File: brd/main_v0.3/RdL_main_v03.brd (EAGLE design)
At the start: 45 x 33.7 mm, 33 parts, among them U1 MPU-6000QFN-24

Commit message: Version Ready for fabrication
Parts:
- removed TEST: PRG, SparkFun-Connectors:1X01_POGOPIN_HOLE_0.58
- added J1: Test, SparkFun-Connectors:1X01
- moved COMM 25.7 mm to (23.2, 28.9)
- moved RT1 21.7 mm to (6.56, 2.50), turned to 0 degrees
- moved BSUPLY 19.6 mm to (2.48, 22.5), turned to 270 degrees
- moved RBUTTON 13.2 mm to (22.1, 19.1), turned to 90 degrees
- moved RT2 11.6 mm to (33.4, 2.28), turned to 180 degrees
- moved BUTTON 11.2 mm to (25.9, 2.50)
- moved D2 11.1 mm to (40.7, 14.2)
- moved R1T1 8.72 mm to (40.7, 8.30), turned to 270 degrees
- moved R10 5.58 mm to (40.6, 22.3), turned to 90 degrees
- moved VT2 3.86 mm to (36.5, 6.99), turned to 0 degrees
- moved CVDD 2.79 mm to (24.0, 23.8)
- moved R3T1 2.71 mm to (2.48, 6.90)
- moved D1 2.71 mm to (2.48, 14.2)
- moved J2 2.70 mm to (6.20, 28.9)
- moved LEDCHARGER 2.70 mm to (8.90, 20.9)
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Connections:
- net N$4: now also J1.1; no longer TEST.1
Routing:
- net VCC: track 5.87 -> 111.6 mm, vias 0 -> 4
- net GND: track 23.1 -> 95.6 mm, vias 0 -> 6
- net N$22: track 0.00 -> 49.4 mm, vias 0 -> 2
- net N$20: track 0.00 -> 41.6 mm, vias 0 -> 3
- net N$10: track 0.00 -> 31.1 mm, vias 0 -> 2
- net N$1: track 0.00 -> 21.7 mm, vias 0 -> 2
- net N$15: track 0.00 -> 21.1 mm, vias 0 -> 2
- net N$18: track 0.00 -> 21.1 mm
- net N$2: track 15.3 -> 35.6 mm, vias 0 -> 2
- net N$12: track 0.00 -> 10.2 mm, vias 0 -> 2
- net N$11: track 0.00 -> 8.83 mm
- net N$5: track 22.2 -> 14.1 mm
- net N$8: track 0.00 -> 5.74 mm
- net N$6: track 0.00 -> 4.72 mm
- net N$14: track 0.00 -> 4.40 mm
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- added copper zone on layer 16, net GND
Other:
- board size 45 x 33.7 mm -> 44 x 31 mm
- board text added: "RdL main v0.3"

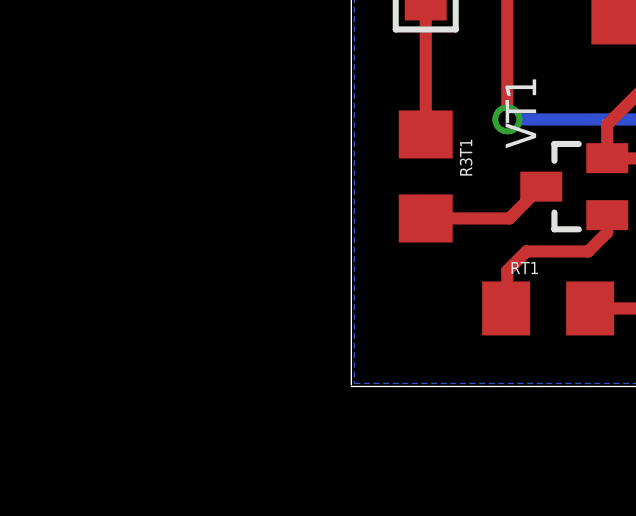
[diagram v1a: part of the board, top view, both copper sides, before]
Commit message: Added version 4 to divide in 3 boards
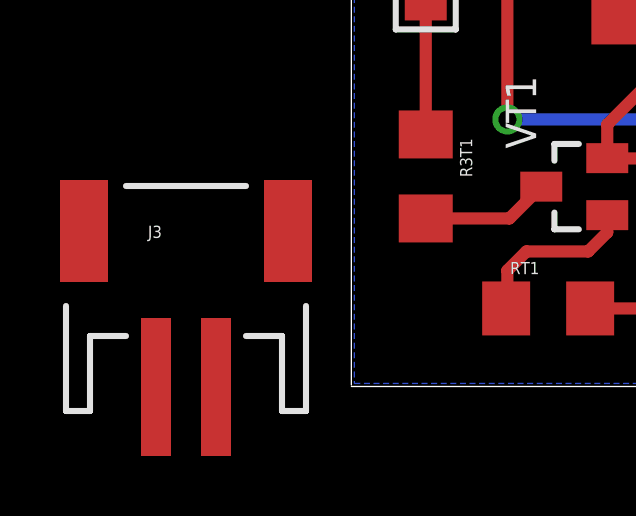
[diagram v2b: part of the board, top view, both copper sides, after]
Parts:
- added J3: (no value), SparkFun-Connectors:JST-2-SMD
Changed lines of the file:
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@@
 <element name="J2" library="SparkFun-Connectors" package="USB-AB-MICRO-SMD" value="" x="6.2" y="28.9" rot="R270"/>
 <element name="J1" library="SparkFun-Connectors" package="1X01" value="Test" x="35.5" y="11.1"/>
+<element name="J3" library="SparkFun-Connectors" package="JST-2-SMD" value="" x="-5.5118" y="3.5814">
+<attribute name="PROD_ID" value="CONN-11443" x="-5.5118" y="3.5814" size="1.778" layer="27" display="off"/>
+</element>
 </elements>
 <signals>
